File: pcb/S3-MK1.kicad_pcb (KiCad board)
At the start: 2 copper layers, 4 parts, among them U1 WEMOS_D1_mini, U2 DHT11

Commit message: journal 4 : added, connected new sym, footprints
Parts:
- added BT1: Battery_Cell, custom_footprints_1:Battery_LiPo_Custom, F.Cu at (52.5, 129.0)
- added BZ1: Buzzer, Buzzer_Beeper:Buzzer_TDK_PS1240P02BT_D12.2mm_H6.5mm, F.Cu at (44.0, 52.5)
- added D1: NeoPixel_THT, LED_SMD:LED_SK6812_PLCC4_5.0x5.0mm_P3.2mm, F.Cu at (80.5, 38.4)
- added J1: ~, custom_footprints_1:LD2420_custom, F.Cu at (105.0, 60.3)
- added J2: SW_420, custom_footprints_1:Vibration_sensor_SW420_custom, F.Cu at (37.5, 89.5)
- added R2: R, Resistor_THT:R_Axial_DIN0204_L3.6mm_D1.6mm_P5.08mm_Horizontal, F.Cu at (161.1, 21.5)
- added SW1: SW_Slide_DPDT, Button_Switch_THT:SW_CK_JS202011CQN_DPDT_Straight, F.Cu at (49.5, 106.7)
- moved R1 59.5 mm to (165.5, 32.5)
- moved A1 58.0 mm to (121.2, 52.6)
- moved U2 27.0 mm to (124.0, 79.0), turned to 90 degrees
- moved U1 24.3 mm to (93.1, 84.7)
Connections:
- A1 pad 1: unconnected-(A1-VCC-Pad1) -> Net-(A1-VCC)
- A1 pad 2: unconnected-(A1-GND-Pad2) -> Net-(A1-GND)
- A1 pad 3: unconnected-(A1-SCL-Pad3) -> Net-(A1-SCL)
- A1 pad 4: unconnected-(A1-SDA-Pad4) -> Net-(A1-SDA)
- R1 pad 1: unconnected-(R1-Pad1) -> Net-(U1-A0)
- R1 pad 2: unconnected-(R1-Pad2) -> Net-(A1-VCC)
- U1 pad 10: unconnected-(U1-GND-Pad10) -> Net-(A1-GND)
- U1 pad 11: unconnected-(U1-D4-Pad11) -> Net-(D1-DIN)
- U1 pad 12: unconnected-(U1-D3-Pad12) -> Net-(U1-D3)
- U1 pad 13: unconnected-(U1-SDA/D2-Pad13) -> Net-(A1-SDA)
- U1 pad 14: unconnected-(U1-SCL/D1-Pad14) -> Net-(A1-SCL)
- U1 pad 2: unconnected-(U1-A0-Pad2) -> Net-(U1-A0)
- U1 pad 3: unconnected-(U1-D0-Pad3) -> Net-(BZ1--)
- U1 pad 4: unconnected-(U1-SCK/D5-Pad4) -> Net-(J1-RX)
- U1 pad 5: unconnected-(U1-MISO/D6-Pad5) -> Net-(J1-Pin_4)
- U1 pad 6: unconnected-(U1-MOSI/D7-Pad6) -> Net-(J2-D0)
- U1 pad 8: unconnected-(U1-3V3-Pad8) -> Net-(A1-VCC)
- U2 pad 1: unconnected-(U2-VDD-Pad1) -> Net-(A1-VCC)
- U2 pad 2: unconnected-(U2-DATA-Pad2) -> Net-(U1-D3)
- U2 pad 4: unconnected-(U2-GND-Pad4) -> Net-(A1-GND)

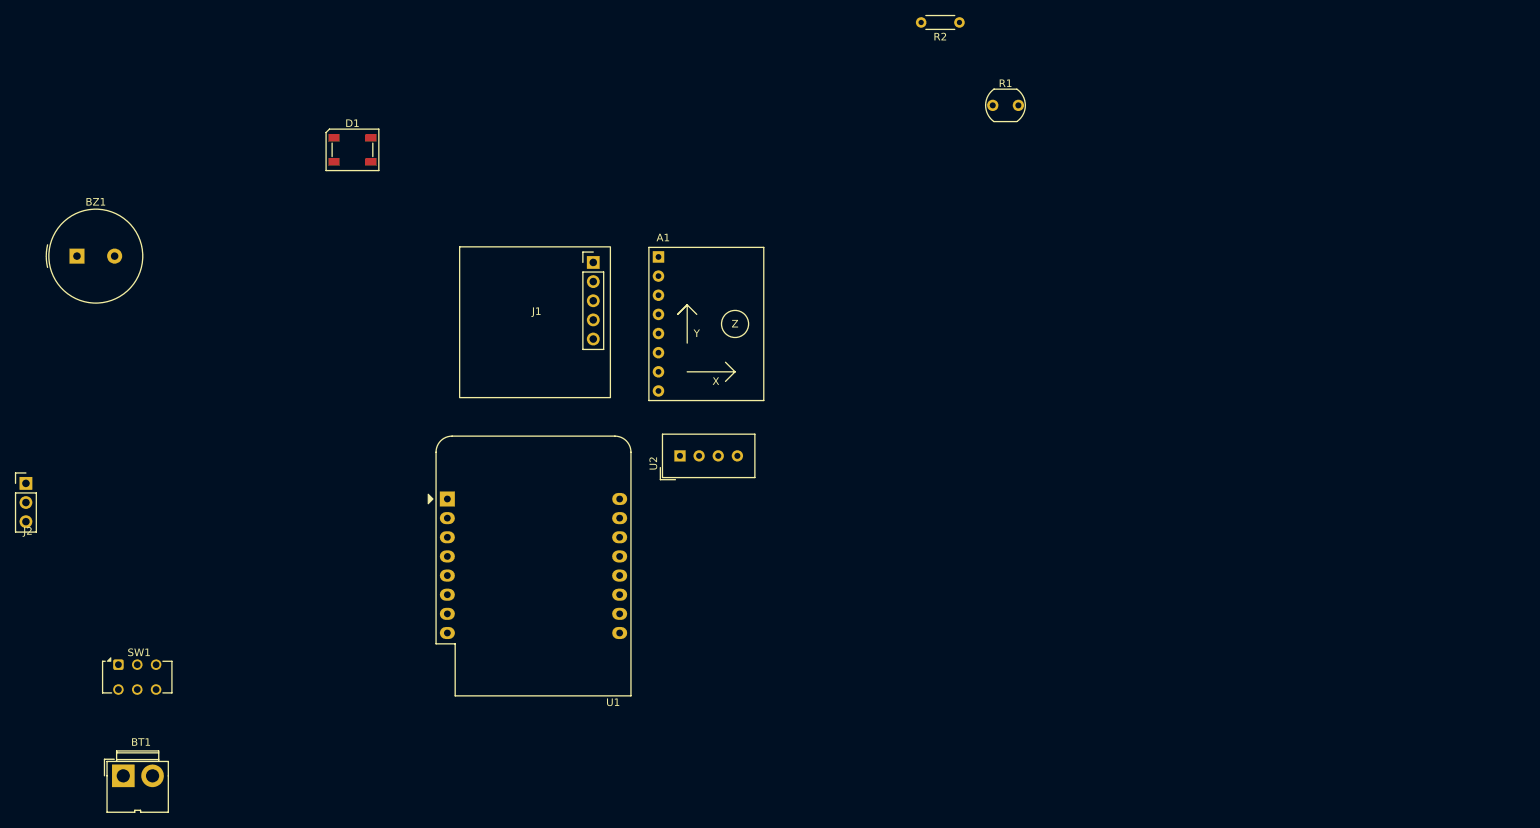
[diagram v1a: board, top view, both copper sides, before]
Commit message: journal 5 : PCB footprints placement
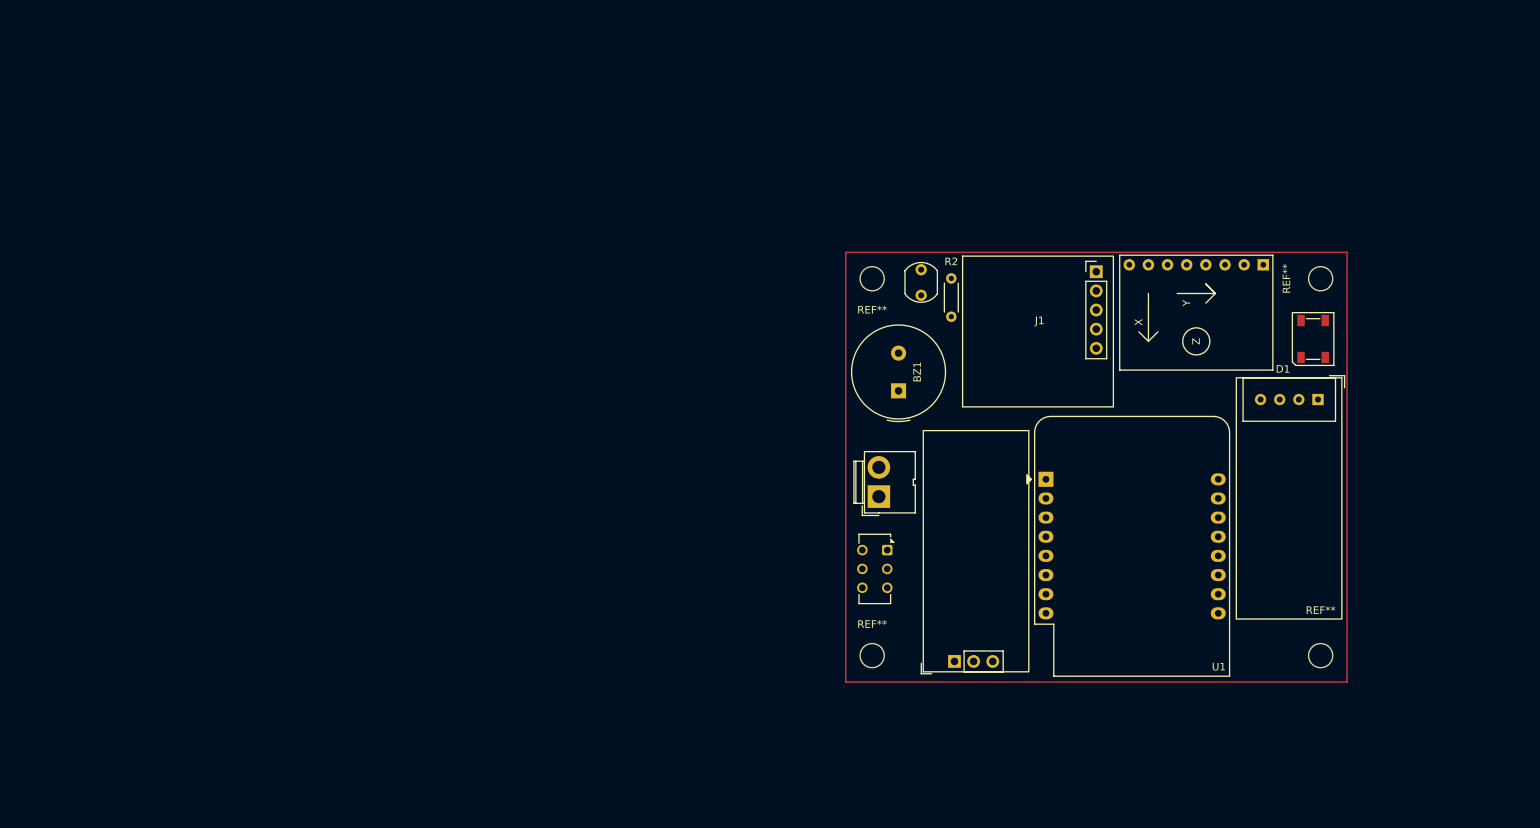
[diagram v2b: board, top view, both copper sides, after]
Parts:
- added REF**: MountingHole_3.2mm_M3, MountingHole:MountingHole_3.2mm_M3, F.Cu at (149.5, 55.5)
- added REF**: MountingHole_3.2mm_M3, MountingHole:MountingHole_3.2mm_M3, F.Cu at (209.0, 55.5)
- added REF**: MountingHole_3.2mm_M3, MountingHole:MountingHole_3.2mm_M3, F.Cu at (149.5, 105.5)
- added REF**: MountingHole_3.2mm_M3, MountingHole:MountingHole_3.2mm_M3, F.Cu at (209.0, 105.5)
- D1: value NeoPixel_THT -> NeoPixel
- moved J2 130.8 mm to (167.3, 106.0), turned to 90 degrees
- moved D1 129.9 mm to (208.0, 63.5), turned to 90 degrees
- moved BT1 115.4 mm to (157.9, 82.1), turned to 90 degrees
- moved BZ1 110.5 mm to (153.0, 70.4), turned to 90 degrees
- moved SW1 103.1 mm to (151.5, 91.5), turned to -90 degrees
- moved U2 85.0 mm to (208.6, 71.5), turned to -90 degrees
- moved A1 80.2 mm to (201.4, 53.6), turned to -90 degrees
- moved U1 79.5 mm to (172.6, 82.1)
- moved J1 66.7 mm to (171.7, 61.6)
- moved R2 39.1 mm to (160.0, 60.5), turned to 90 degrees
- moved R1 23.8 mm to (156.0, 54.3), turned to -90 degrees

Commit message: routed the pcb, solved all errors, journal 6
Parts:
- moved A1 40.3 mm to (164.4, 69.7)
- moved BT1 40.3 mm to (120.9, 98.1)
- moved BZ1 40.3 mm to (116.0, 86.4)
- moved D1 40.3 mm to (171.0, 79.5)
- moved J1 40.3 mm to (134.7, 77.6)
- moved J2 40.3 mm to (130.3, 122.0)
- moved R1 40.3 mm to (119.0, 70.3)
- moved R2 40.3 mm to (123.0, 76.5)
- moved REF** 40.3 mm to (112.5, 71.5)
- moved REF** 40.3 mm to (172.0, 71.5)
- moved REF** 40.3 mm to (112.5, 121.5)
- moved REF** 40.3 mm to (172.0, 121.5)
- moved SW1 40.3 mm to (114.5, 107.5)
- moved U1 40.3 mm to (135.6, 98.1)
- moved U2 40.3 mm to (171.6, 87.5)
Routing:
- net Net-(A1-GND): track 0.00 -> 195.9 mm
- net Net-(A1-VCC): track 0.00 -> 161.0 mm
- net Net-(U1-A0): track 0.00 -> 41.8 mm
- net Net-(D1-DIN): track 0.00 -> 39.5 mm
- net Net-(U1-D3): track 0.00 -> 39.4 mm
- net Net-(J1-RX): track 0.00 -> 38.0 mm
- net Net-(J1-Pin_4): track 0.00 -> 36.8 mm
- net Net-(A1-SDA): track 0.00 -> 36.8 mm
- net Net-(A1-SCL): track 0.00 -> 34.5 mm
- net Net-(BZ1--): track 0.00 -> 29.9 mm
- net Net-(J2-D0): track 0.00 -> 14.4 mm
- net Net-(BT1-+): track 0.00 -> 10.5 mm
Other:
- board outline added: 67.5 x 58 mm

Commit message: journal 7 : added new components, firmware
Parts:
- D1: value NeoPixel -> NeoPixel_THT
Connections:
- R1 pad 1: Net-(U1-A0) -> Net-(U1-CS/D8)
- R2 pad 2: Net-(U1-A0) -> Net-(U1-CS/D8)
- U1 pad 2: Net-(U1-A0) -> Net-(J3-Pin_3)
- U1 pad 7: unconnected-(U1-CS/D8-Pad7) -> Net-(U1-CS/D8)
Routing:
- net Net-(U1-CS/D8): track 0.00 -> 47.1 mm
- net Net-(U1-A0): track 41.8 -> 0.00 mm
- net (no net): track 0.00 -> 41.8 mm
- net Net-(J2-D0): track 14.4 -> 17.0 mm
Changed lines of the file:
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@@
 		(sheetname "/")
 		(sheetfile "S3-MK1.kicad_sch")
+		(units
+			(unit
+				(name "A")
+				(pins "1" "2" "3")
+			)
+		)
 		(attr through_hole)
 		(duplicate_pad_numbers_are_jumpers no)
@@
 			(layers "*.Cu" "*.Mask")
 			(remove_unused_layers no)
-			(net "Net-(U1-A0)")
+			(net "Net-(U1-CS{slash}D8)")
 			(pintype "passive")
 		)
@@
 		(sheetname "/")
 		(sheetfile "S3-MK1.kicad_sch")
+		(units
+			(unit
+				(name "A")
+				(pins "1" "15" "16" "9" "10" "8" "2" "3" "14" "13" "12" "11" "4" "5"
+					"6" "7"
+				)
+			)
+		)
 		(attr through_hole)
 		(duplicate_pad_numbers_are_jumpers no)
@@
 			(layers "*.Cu" "*.Mask")
 			(remove_unused_layers no)
-			(net "Net-(U1-A0)")
+			(net "Net-(J3-Pin_3)")
 			(pinfunction "A0_2")
 			(pintype "input")
@@
 			(layers "*.Cu" "*.Mask")
 			(remove_unused_layers no)
-			(net "unconnected-(U1-CS{slash}D8-Pad7)")
+			(net "Net-(U1-CS{slash}D8)")
 			(pinfunction "CS/D8_7")
 			(pintype "bidirectional")
@@
 			)
 		)
-		(property "Value" "NeoPixel"
+		(property "Value" "NeoPixel_THT"
 			(at 0 4 90)
 			(layer "F.Fab")
@@
 			(layers "*.Cu" "*.Mask")
 			(remove_unused_layers no)
-			(net "Net-(U1-A0)")
+			(net "Net-(U1-CS{slash}D8)")
 			(pintype "passive")
 		)
@@
 		(sheetname "/")
 		(sheetfile "S3-MK1.kicad_sch")
+		(units
+			(unit
+				(name "A")
+				(pins "3" "1" "4" "2")
+			)
+		)
 		(attr through_hole)
 		(duplicate_pad_numbers_are_jumpers no)
@@
 	)
 	(segment
+		(start 119 70.3)
+		(end 121.84 70.3)
+		(width 0.2)
+		(layer "F.Cu")
+		(net "")
+	)
+	(segment
+		(start 135.555 100.65)
+		(end 119.5 84.595)
+		(width 0.2)
+		(layer "F.Cu")
+		(net "")
+	)
+	(segment
+		(start 119.5 84.595)
+		(end 119.5 74.96)
+		(width 0.2)
+		(layer "F.Cu")
+		(net "")
+	)
+	(segment
+		(start 121.84 70.3)
+		(end 123 71.46)
+		(width 0.2)
+		(layer "F.Cu")
+		(net "")
+	)
+	(segment
+		(start 119.5 74.96)
+		(end 123 71.46)
+		(width 0.2)
+		(layer "F.Cu")
+		(net "")
+	)
+	(segment
 		(start 111.2 110)
 		(end 113.3875 107.8125)
@@
 	)
 	(segment
-		(start 128.5 117.865)
-		(end 135.555 110.81)
+		(start 134.849365 114.5)
+		(end 136.5 114.5)
 		(width 0.2)
 		(layer "F.Cu")
@@
 	)
 	(segment
-		(start 128.5 122.27)
-		(end 128.5 117.865)
+		(start 137 114)
+		(end 137 111.5)
 		(width 0.2)
 		(layer "F.Cu")
@@
 	)
 	(segment
-		(start 119 70.3)
-		(end 121.84 70.3)
+		(start 128.5 122.27)
+		(end 128.5 120.849365)
 		(width 0.2)
 		(layer "F.Cu")
-		(net "Net-(U1-A0)")
+		(net "Net-(J2-D0)")
 	)
 	(segment
-		(start 135.555 100.65)
-		(end 119.5 84.595)
+		(start 128.5 120.849365)
+		(end 134.849365 114.5)
 		(width 0.2)
 		(layer "F.Cu")
-		(net "Net-(U1-A0)")
+		(net "Net-(J2-D0)")
 	)
 	(segment
-		(start 119.5 84.595)
-		(end 119.5 74.96)
+		(start 136.31 110.81)
+		(end 135.555 110.81)
 		(width 0.2)
 		(layer "F.Cu")
-		(net "Net-(U1-A0)")
+		(net "Net-(J2-D0)")
 	)
 	(segment
-		(start 121.84 70.3)
-		(end 123 71.46)
+		(start 137 111.5)
+		(end 136.31 110.81)
 		(width 0.2)
 		(layer "F.Cu")
-		(net "Net-(U1-A0)")
+		(net "Net-(J2-D0)")
 	)
 	(segment
-		(start 119.5 74.96)
-		(end 123 71.46)
+		(start 136.5 114.5)
+		(end 137 114)
 		(width 0.2)
 		(layer "F.Cu")
-		(net "Net-(U1-A0)")
+		(net "Net-(J2-D0)")
 	)
 	(segment
@@
 		(net "Net-(A1-SCL)")
 	)
+	(segment
+		(start 128 105.795)
+		(end 128 76.46)
+		(width 0.2)
+		(layer "B.Cu")
+		(net "Net-(U1-CS{slash}D8)")
+	)
+	(segment
+		(start 135.555 113.35)
+		(end 128 105.795)
+		(width 0.2)
+		(layer "B.Cu")
+		(net "Net-(U1-CS{slash}D8)")
+	)
+	(segment
+		(start 128 76.46)
+		(end 123 71.46)
+		(width 0.2)
+		(layer "B.Cu")
+		(net "Net-(U1-CS{slash}D8)")
+	)
 	(embedded_fonts no)

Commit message: added journal 8, pcb files, libs
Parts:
- added J3: audio, custom_footprints_1:Audio_sensor_custom, F.Cu at (155.0, 86.1)
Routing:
- net Net-(J3-Pin_3): track 0.00 -> 25.1 mm
- net Net-(A1-VCC): track 161.0 -> 179.4 mm
- net Net-(A1-GND): track 195.9 -> 209.5 mm

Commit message: journal 9, added S3 watch PCB, files
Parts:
- added BT2: Battery_Cell, custom_footprints_1:Battery_LiPo_Custom, F.Cu at (229.0, 79.0)
- added BZ2: Buzzer, Buzzer_Beeper:MagneticBuzzer_Kingstate_KCG0601, F.Cu at (227.0, 97.5)
- added BZ3: Haptic_Vibration, Buzzer_Beeper:MagneticBuzzer_Kingstate_KCG0601, F.Cu at (214.9, 97.5)
- added D2: NeoPixel_THT, LED_SMD:LED_SK6812_PLCC4_5.0x5.0mm_P3.2mm, F.Cu at (222.6, 114.0)
- added J5: OLED_128x64, ScottoKeebs_Scotto:OLED_128x64, F.Cu at (222.5, 96.7)
- added SW2: SW_Slide_DPDT, Button_Switch_THT:SW_CK_JS202011CQN_DPDT_Straight, F.Cu at (213.0, 84.7)
- added SW3: SW_Push, Button_Switch_THT:SW_PUSH_1P1T_6x3.5mm_H4.3_APEM_MJTP1243, F.Cu at (211.2, 112.5)
- added SW4: SW_Push, Button_Switch_THT:SW_PUSH_1P1T_6x3.5mm_H4.3_APEM_MJTP1243, F.Cu at (234.0, 112.5)
- added SW5: SW_Push, Button_Switch_THT:SW_PUSH_1P1T_6x3.5mm_H4.3_APEM_MJTP1243, F.Cu at (234.0, 117.0)
- added SW6: SW_Push, Button_Switch_THT:SW_PUSH_1P1T_6x3.5mm_H4.3_APEM_MJTP1243, F.Cu at (211.2, 117.0)
- added U3: WEMOS_D1_mini, RF_Module:WEMOS_D1_mini_light, B.Cu at (233.9, 91.1)
- J3: value audio -> audio_sensor_custom
- moved J2 46.1 mm to (85.3, 112.0)
- moved BT1 46.1 mm to (75.9, 88.1)
- moved BZ1 46.1 mm to (71.0, 76.4)
- moved D1 46.1 mm to (126.0, 69.5)
- moved J3 46.1 mm to (110.0, 76.1)
- moved R1 46.1 mm to (74.0, 60.3)
- moved R2 46.1 mm to (78.0, 66.5)
- moved REF** 46.1 mm to (67.5, 61.5)
- moved REF** 46.1 mm to (127.0, 61.5)
- moved REF** 46.1 mm to (67.5, 111.5)
- moved REF** 46.1 mm to (127.0, 111.5)
- moved SW1 46.1 mm to (69.5, 97.5)
- moved U1 46.1 mm to (90.6, 88.1)
- moved U2 46.1 mm to (126.6, 77.5)
- moved A1 46.1 mm to (119.4, 59.6)
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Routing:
- net (no net): track 41.8 -> 0.00 mm
- net Net-(U1-CS/D8): track 47.1 -> 51.2 mm
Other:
- board size 67.5 x 58 mm -> 172.5 x 62 mm

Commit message: journal 10, added pcb, complete  s3 watch files
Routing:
- net Net-(BT2--): track 0.00 -> 73.7 mm
- net Net-(U3-CS/D8): track 0.00 -> 59.7 mm
- net Net-(U3-D0): track 0.00 -> 47.9 mm
- net Net-(J5-VCC): track 0.00 -> 39.1 mm
- net Net-(U3-D4): track 0.00 -> 26.5 mm
- net Net-(BZ3-+): track 0.00 -> 22.0 mm
- net Net-(D2-DIN): track 0.00 -> 21.8 mm
- net Net-(J5-SCL): track 0.00 -> 20.5 mm
- net Net-(BT2-+): track 0.00 -> 19.0 mm
- net Net-(U3-D3): track 0.00 -> 16.9 mm
- net Net-(J5-SDA): track 0.00 -> 12.7 mm
- net Net-(BZ2-+): track 0.00 -> 8.49 mm
- net Net-(A1-VCC): track 179.4 -> 178.8 mm
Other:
- board size 172.5 x 62 mm -> 172.5 x 66 mm
